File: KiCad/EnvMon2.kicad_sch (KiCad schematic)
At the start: 28 parts, among them J1 USB-C, J2 DC, M1 OLED1.5-RGB, U1 LMR16006+FB, U2 SCD41, U3 FT231XQ, U4 DS18B20, U5 ESP32-PICO-MINI-02, U6 QR

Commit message: Making progress
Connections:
- net D+: now also U3.8 (USBDP)
- net D-: no longer U3.8 (USBDP)
- net TEMP: now also U5.24 (IO4)
- no-connect marks 5 -> 6
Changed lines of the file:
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@@
   (junction (at 43.18 131.445) (diameter 0) (color 0 0 0 0)
   )
+  (junction (at 55.88 40.64) (diameter 0) (color 0 0 0 0)
+  )
   (junction (at 114.3 27.94) (diameter 0) (color 0 0 0 0)
   )
@@
   )
   (junction (at 49.53 141.605) (diameter 0) (color 0 0 0 0)
+  )
+  (junction (at 55.88 48.26) (diameter 0) (color 0 0 0 0)
   )
   (junction (at 38.735 139.065) (diameter 0) (color 0 0 0 0)
@@
   (no_connect (at 149.86 53.34))
   (no_connect (at 55.88 55.88))
+  (no_connect (at 58.42 99.06))
   (no_connect (at 55.88 58.42))
   (wire (pts (xy 55.88 33.02) (xy 58.42 33.02))
@@
     (stroke (width 0) (type default) (color 0 0 0 0))
   )
+  (wire (pts (xy 55.88 48.26) (xy 58.42 48.26))
+    (stroke (width 0) (type default) (color 0 0 0 0))
+  )
   (wire (pts (xy 97.79 91.44) (xy 114.3 91.44))
     (stroke (width 0) (type default) (color 0 0 0 0))
@@
     (stroke (width 0) (type default) (color 0 0 0 0))
   )
+  (wire (pts (xy 55.88 40.64) (xy 58.42 40.64))
+    (stroke (width 0) (type default) (color 0 0 0 0))
+  )
   (wire (pts (xy 114.3 27.94) (xy 114.3 20.32))
     (stroke (width 0) (type default) (color 0 0 0 0))
@@
     (stroke (width 0) (type default) (color 0 0 0 0))
   )
-  (global_label "D-" (shape bidirectional) (at 114.3 38.1 180) (fields_autoplaced)
+  (global_label "D+" (shape bidirectional) (at 114.3 38.1 180) (fields_autoplaced)
     (effects (font (size 1.27 1.27)) (justify right))
     (property "Intersheet References" "${INTERSHEET_REFS}" (id 0) (at 109.1334 38.0206 0)
@@
     )
   )
-  (global_label "D-" (shape bidirectional) (at 55.88 43.18 0) (fields_autoplaced)
-    (effects (font (size 1.27 1.27)) (justify left))
-    (property "Intersheet References" "${INTERSHEET_REFS}" (id 0) (at 61.0466 43.1006 0)
+  (global_label "TEMP" (shape bidirectional) (at 195.58 63.5 180) (fields_autoplaced)
+    (effects (font (size 1.27 1.27)) (justify right))
+    (property "Intersheet References" "${INTERSHEET_REFS}" (id 0) (at 188.4177 63.5794 0)
+      (effects (font (size 1.27 1.27)) (justify right) hide)
+    )
+  )
+  (global_label "D-" (shape bidirectional) (at 58.42 40.64 0) (fields_autoplaced)
+    (effects (font (size 1.27 1.27)) (justify left))
+    (property "Intersheet References" "${INTERSHEET_REFS}" (id 0) (at 63.5866 40.5606 0)
       (effects (font (size 1.27 1.27)) (justify left) hide)
     )
@@
     )
   )
-  (global_label "D+" (shape bidirectional) (at 55.88 45.72 0) (fields_autoplaced)
-    (effects (font (size 1.27 1.27)) (justify left))
-    (property "Intersheet References" "${INTERSHEET_REFS}" (id 0) (at 61.0466 45.6406 0)
-      (effects (font (size 1.27 1.27)) (justify left) hide)
-    )
+  (global_label "D+" (shape bidirectional) (at 58.42 48.26 0) (fields_autoplaced)
+    (effects (font (size 1.27 1.27)) (justify left))
+    (property "Intersheet References" "${INTERSHEET_REFS}" (id 0) (at 63.5866 48.1806 0)
+      (effects (font (size 1.27 1.27)) (justify left) hide)
+    )

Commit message: Ready
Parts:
- added J3: TEMP, RevK:Molex_MiniSPOX_H3RA, symbol Connector_Generic:Conn_01x03
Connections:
- net RX is gone; now on net O: U3.1 (RXD)
- net TX is gone; now on net I: U3.17 (TXD)
- net +3V3: now also J3.3 (Pin_3)
- net B: now also U5.21 (IO15)
- net EN: now also U5.8 (EN)
- net G: now also U5.18 (IO14)
- net GND: now also J3.1 (Pin_1)
- net OLED-CS0: now also U5.28 (IO8)
- net OLED-DC: now also U5.34 (IO22)
- net OLED-MOSI: now also U5.26 (IO20)
- net OLED-RST: now also U5.35 (IO21)
- net OLED-SCLK: now also U5.27 (IO7)
- net R: now also U5.20 (IO13)
- net TEMP: now also J3.2 (Pin_2)
- net BOOT: now reaches U3.18 (~{DTR})
- net BOOT: now also U5.23 (IO0)
- net at U2.1 (DNC), U2.11 (DNC), U2.12 (DNC)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: now also U2.3 (DNC)
- net I: now reaches U5.30 (RXD0)
- net O: now reaches U5.31 (TXD0)

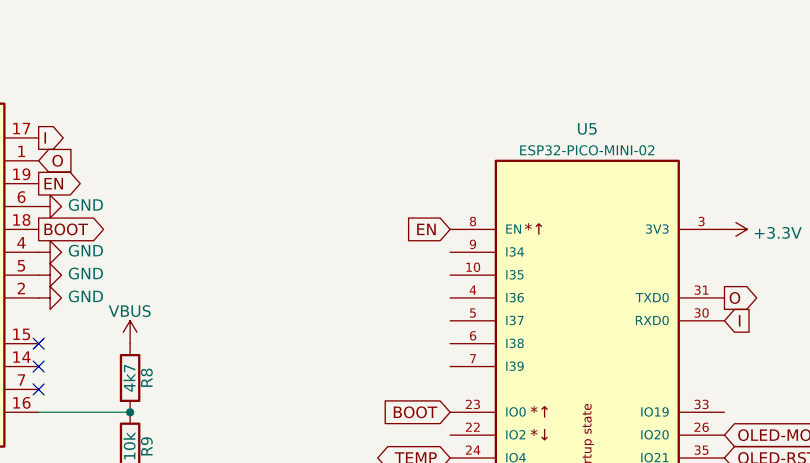
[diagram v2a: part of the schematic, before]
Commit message: Missed a pull up
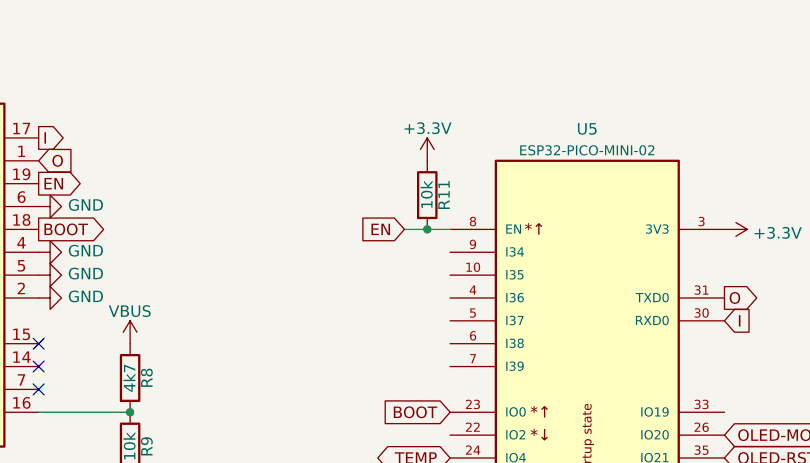
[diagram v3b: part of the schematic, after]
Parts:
- added R11: 10k, RevK:R_0603, symbol Device:R
- J3, M1: now left out of the parts list
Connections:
- net +3V3: now also R11.1
- net EN: now also R11.2
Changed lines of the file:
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@@
   (junction (at 43.18 131.445) (diameter 0) (color 0 0 0 0)
+  )
+  (junction (at 193.04 38.1) (diameter 0) (color 0 0 0 0)
   )
   (junction (at 55.88 40.64) (diameter 0) (color 0 0 0 0)
@@
     (stroke (width 0) (type default) (color 0 0 0 0))
   )
+  (wire (pts (xy 193.04 38.1) (xy 195.58 38.1))
+    (stroke (width 0) (type default) (color 0 0 0 0))
+  )
   (wire (pts (xy 38.735 139.065) (xy 49.53 139.065))
     (stroke (width 0) (type default) (color 0 0 0 0))
@@
   )
   (wire (pts (xy 129.54 66.04) (xy 132.08 66.04))
+    (stroke (width 0) (type default) (color 0 0 0 0))
+  )
+  (wire (pts (xy 190.5 38.1) (xy 193.04 38.1))
     (stroke (width 0) (type default) (color 0 0 0 0))
   )
@@
     )
   )
-  (global_label "EN" (shape input) (at 195.58 38.1 180) (fields_autoplaced)
-    (effects (font (size 1.27 1.27)) (justify right))
-    (property "Intersheet References" "${INTERSHEET_REFS}" (id 0) (at 190.7763 38.0206 0)
+  (global_label "EN" (shape input) (at 190.5 38.1 180) (fields_autoplaced)
+    (effects (font (size 1.27 1.27)) (justify right))
+    (property "Intersheet References" "${INTERSHEET_REFS}" (id 0) (at 185.6963 38.0206 0)
       (effects (font (size 1.27 1.27)) (justify right) hide)
     )
@@
   )
   (symbol (lib_id "RevK:OLED1.5-RGB") (at 114.3 88.9 0) (unit 1)
-    (in_bom yes) (on_board yes)
+    (in_bom no) (on_board yes)
     (property "Reference" "M1" (id 0) (at 146.7612 97.7646 0)
       (effects (font (size 1.27 1.27)) (justify left))
@@
   (symbol (lib_id "power:GND") (at 198.12 132.08 270) (unit 1)
     (in_bom yes) (on_board yes) (fields_autoplaced)
-    (property "Reference" "#PWR023" (id 0) (at 191.77 132.08 0)
+    (property "Reference" "#PWR024" (id 0) (at 191.77 132.08 0)
       (effects (font (size 1.27 1.27)) hide)
     )
@@
   )
   (symbol (lib_id "Connector_Generic:Conn_01x03") (at 203.2 134.62 0) (unit 1)
+    (in_bom no) (on_board yes) (fields_autoplaced)
+    (property "Reference" "J3" (id 0) (at 205.232 133.7853 0)
+      (effects (font (size 1.27 1.27)) (justify left))
+    )
+    (property "Value" "TEMP" (id 1) (at 205.232 136.3222 0)
+      (effects (font (size 1.27 1.27)) (justify left))
+    )
+    (property "Footprint" "RevK:Molex_MiniSPOX_H3RA" (id 2) (at 203.2 134.62 0)
+      (effects (font (size 1.27 1.27)) hide)
+    )
+    (property "Datasheet" "~" (id 3) (at 203.2 134.62 0)
+      (effects (font (size 1.27 1.27)) hide)
+    )
+    (pin "1")
+    (pin "2")
+    (pin "3")
+  )
+  (symbol (lib_id "power:GND") (at 86.995 33.02 90) (unit 1)
+    (in_bom yes) (on_board yes)
+    (property "Reference" "#PWR09" (id 0) (at 93.345 33.02 0)
+      (effects (font (size 1.27 1.27)) hide)
+    )
+    (property "Value" "GND" (id 1) (at 90.2462 32.893 90)
+      (effects (font (size 1.27 1.27)) (justify right))
+    )
+    (property "Footprint" "" (id 2) (at 86.995 33.02 0)
+      (effects (font (size 1.27 1.27)) hide)
+    )
+    (property "Datasheet" "" (id 3) (at 86.995 33.02 0)
+      (effects (font (size 1.27 1.27)) hide)
+    )
+    (pin "1")
+  )
+  (symbol (lib_id "power:+3.3V") (at 193.04 30.48 0) (unit 1)
     (in_bom yes) (on_board yes) (fields_autoplaced)
-    (property "Reference" "J3" (id 0) (at 205.232 133.7853 0)
-      (effects (font (size 1.27 1.27)) (justify left))
-    )
-    (property "Value" "TEMP" (id 1) (at 205.232 136.3222 0)
-      (effects (font (size 1.27 1.27)) (justify left))
-    )
-    (property "Footprint" "RevK:Molex_MiniSPOX_H3RA" (id 2) (at 203.2 134.62 0)
-      (effects (font (size 1.27 1.27)) hide)
-    )
-    (property "Datasheet" "~" (id 3) (at 203.2 134.62 0)
-      (effects (font (size 1.27 1.27)) hide)
-    )
-    (pin "1")
-    (pin "2")
-    (pin "3")
-  )
-  (symbol (lib_id "power:GND") (at 86.995 33.02 90) (unit 1)
-    (in_bom yes) (on_board yes)
-    (property "Reference" "#PWR09" (id 0) (at 93.345 33.02 0)
-      (effects (font (size 1.27 1.27)) hide)
-    )
-    (property "Value" "GND" (id 1) (at 90.2462 32.893 90)
-      (effects (font (size 1.27 1.27)) (justify right))
-    )
-    (property "Footprint" "" (id 2) (at 86.995 33.02 0)
-      (effects (font (size 1.27 1.27)) hide)
-    )
-    (property "Datasheet" "" (id 3) (at 86.995 33.02 0)
+    (property "Reference" "#PWR023" (id 0) (at 193.04 34.29 0)
+      (effects (font (size 1.27 1.27)) hide)
+    )
+    (property "Value" "+3.3V" (id 1) (at 193.04 26.9042 0))
+    (property "Footprint" "" (id 2) (at 193.04 30.48 0)
+      (effects (font (size 1.27 1.27)) hide)
+    )
+    (property "Datasheet" "" (id 3) (at 193.04 30.48 0)
       (effects (font (size 1.27 1.27)) hide)
     )
@@
   (symbol (lib_id "power:GND") (at 226.06 88.9 90) (unit 1)
     (in_bom yes) (on_board yes) (fields_autoplaced)
-    (property "Reference" "#PWR026" (id 0) (at 232.41 88.9 0)
+    (property "Reference" "#PWR027" (id 0) (at 232.41 88.9 0)
       (effects (font (size 1.27 1.27)) hide)
     )
@@
   (symbol (lib_id "power:+3.3V") (at 198.12 137.16 90) (unit 1)
     (in_bom yes) (on_board yes) (fields_autoplaced)
-    (property "Reference" "#PWR024" (id 0) (at 201.93 137.16 0)
+    (property "Reference" "#PWR025" (id 0) (at 201.93 137.16 0)
       (effects (font (size 1.27 1.27)) hide)
     )
@@
     )
     (property "Datasheet" "~" (id 3) (at 83.185 33.02 0)
+      (effects (font (size 1.27 1.27)) hide)
+    )
+    (pin "1")
+    (pin "2")
+  )
+  (symbol (lib_id "Device:R") (at 193.04 34.29 0) (unit 1)
+    (in_bom yes) (on_board yes)
+    (property "Reference" "R11" (id 0) (at 194.945 34.29 90))
+    (property "Value" "10k" (id 1) (at 193.04 34.29 90))
+    (property "Footprint" "RevK:R_0603" (id 2) (at 191.262 34.29 90)
+      (effects (font (size 1.27 1.27)) hide)
+    )
+    (property "Datasheet" "~" (id 3) (at 193.04 34.29 0)
       (effects (font (size 1.27 1.27)) hide)
     )
@@
   (symbol (lib_id "power:+3.3V") (at 226.06 38.1 270) (unit 1)
     (in_bom yes) (on_board yes) (fields_autoplaced)
-    (property "Reference" "#PWR025" (id 0) (at 222.25 38.1 0)
+    (property "Reference" "#PWR026" (id 0) (at 222.25 38.1 0)
       (effects (font (size 1.27 1.27)) hide)
     )
@@
       (reference "#PWR022") (unit 1) (value "GND") (footprint "")
     )
+    (path "/3bb9ffa2-b3c1-4e1c-bce6-7c8ab391c7f1"
+      (reference "#PWR023") (unit 1) (value "+3.3V") (footprint "")
+    )
     (path "/1a8ea755-9b15-40ee-9e6d-e6e4769aa2cc"
-      (reference "#PWR023") (unit 1) (value "GND") (footprint "")
+      (reference "#PWR024") (unit 1) (value "GND") (footprint "")
     )
     (path "/4d3b3a19-358a-434b-b4e1-15f15982ced7"
-      (reference "#PWR024") (unit 1) (value "+3.3V") (footprint "")
+      (reference "#PWR025") (unit 1) (value "+3.3V") (footprint "")
     )
     (path "/d11ded20-64d4-49f4-9ed1-1e95f6ee0a71"
-      (reference "#PWR025") (unit 1) (value "+3.3V") (footprint "")
+      (reference "#PWR026") (unit 1) (value "+3.3V") (footprint "")
     )
     (path "/3d47db6c-7329-4ec7-99d8-dfde5d30f830"
-      (reference "#PWR026") (unit 1) (value "GND") (footprint "")
+      (reference "#PWR027") (unit 1) (value "GND") (footprint "")
     )
     (path "/00000000-0000-0000-0000-0000610f9b88"
@@
       (reference "R10") (unit 1) (value "4k7") (footprint "Resistor_SMD:R_0603_1608Metric_Pad0.98x0.95mm_HandSolder")
     )
+    (path "/90b8eaac-a159-4dee-976f-dbdad4d50f22"
+      (reference "R11") (unit 1) (value "10k") (footprint "RevK:R_0603")
+    )
     (path "/7cbfa237-177e-4c8c-8cb5-2871c201d869"

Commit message: Clean footprint
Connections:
- net GND: no longer U5.54 (GND), U5.55 (GND), U5.56 (GND), U5.57 (GND), U5.58 (GND), U5.59 (GND), U5.60 (GND), U5.61 (GND)
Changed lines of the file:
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@@
     (pin "52")
     (pin "53")
-    (pin "54")
-    (pin "55")
-    (pin "56")
-    (pin "57")
-    (pin "58")
-    (pin "59")
     (pin "6")
-    (pin "60")
-    (pin "61")
     (pin "7")
     (pin "8")
